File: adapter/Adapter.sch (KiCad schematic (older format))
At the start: 54 parts, among them J1 USB_B_Micro, J2 2040210-1, J3 USB_C_Receptacle, J4 Conn_01x05_Male, J5 Conn_01x03_Male, Q1 IRLML2244TRPBF, SW1 RESET, SW2 BOOT, U2 LD1117S33TR, U3 STM32F072C8Tx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

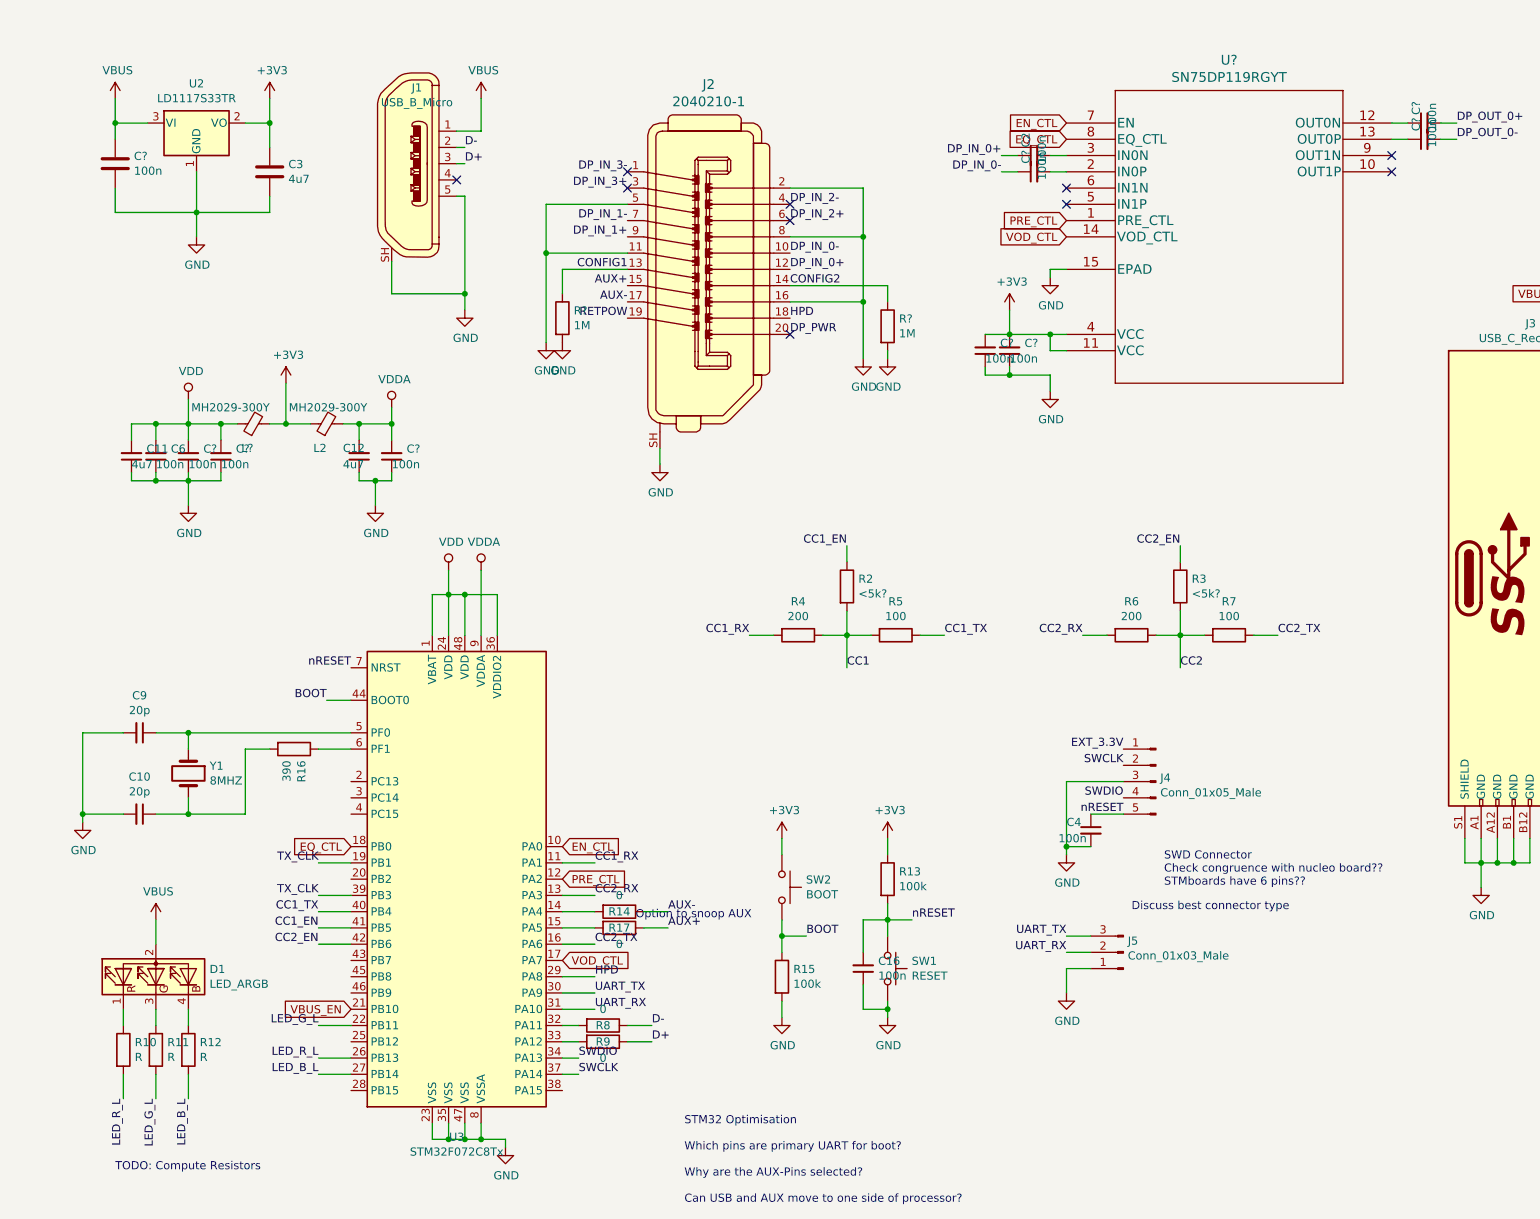
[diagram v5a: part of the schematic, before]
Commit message: cleared all order number for Arrow
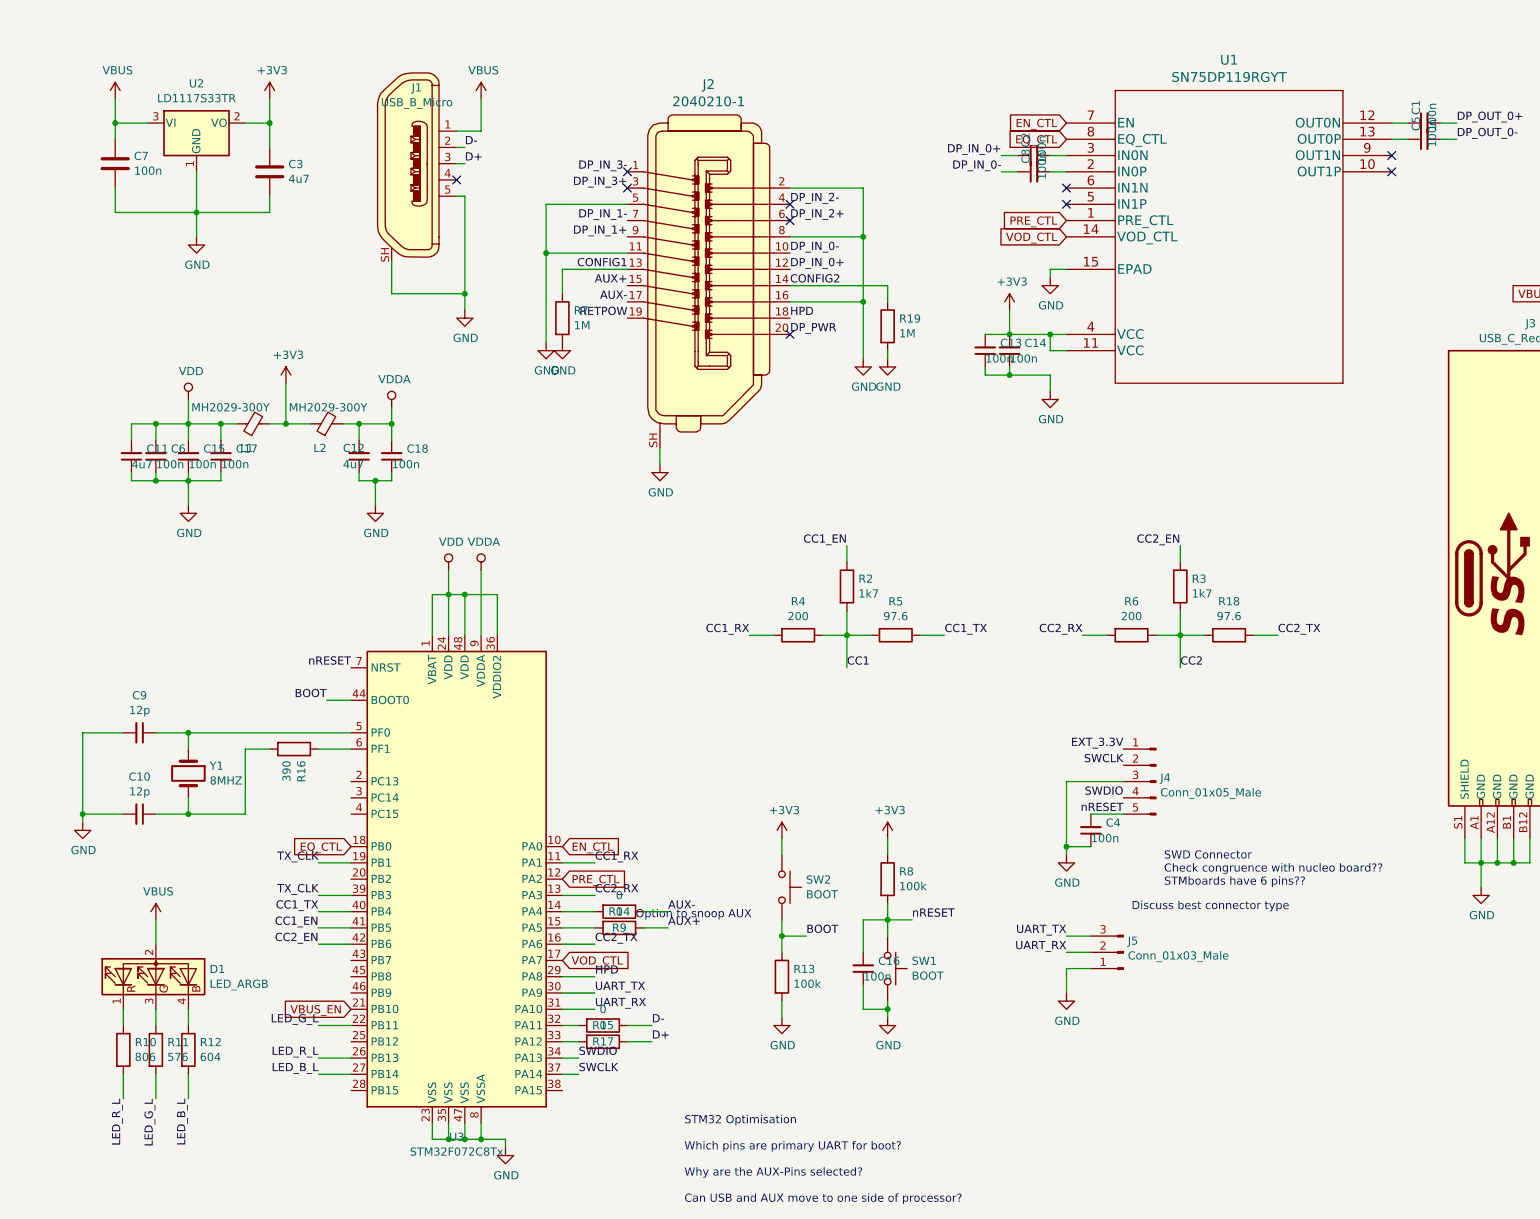
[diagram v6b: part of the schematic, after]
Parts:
- removed R?: 1M, symbol Device:R
- added R18: 97.6, Resistor_SMD:R_0603_1608Metric_Pad1.05x0.95mm_HandSolder, symbol Device:R
- C10, C9: value 20p -> 12p; MFP CC0603JRNPO9BN120 -> CL10C120JB8NNNC; S2PN (none) -> CL10C120JB8NNNC
- C16, C4: S2PN (none) -> CL10F104ZO8NNNC
- D1: S2PN (none) -> CLVBA-FKA-CAEDH8BBB7a363
- R1: S2PN (none) -> CRCW0603100KJNEAC
- R10: value R -> 806; MFP (none) -> RC0603FR-07806RL; S2PN (none) -> RC0603FR-07806RL
- R11: value R -> 576; MFP (none) -> RMCF0603FT576R; S2PN (none) -> RMCF0603FT576R
- R12: value R -> 604; MFP (none) -> RC0603FR-07604RL; S2PN (none) -> RC0603FR-07604RL
- R13: MFP RC0603FR-13100KL -> (none); S2PN (none) -> CRCW0603100KJNEAC
- R14, R17, R9: MFP (none) -> RC0603JR-070RL; S2PN (none) -> RC0603JR-070RL
- R15: value 100k -> 0; MFP RC0603FR-13100KL -> RC0603JR-070RL; S2PN (none) -> RC0603JR-070RL
- R16: MFP (none) -> RC0603JR-07390RL; S2PN (none) -> RC0603JR-07390RL
- R19: renamed from R?; footprint (none) -> Resistor_SMD:R_0603_1608Metric_Pad1.05x0.95mm_HandSolder; MFP (none) -> AC0603JR-071ML; S2PN RC0603FR-101ML -> AC0603JR-071ML
- R2, R3: value <5k? -> 1k7; MFP (none) -> RC0603FR-071K69L; S2PN (none) -> RC0603FR-071K69L
- R4, R6: MFP (none) -> RC0603FR-07200RL; S2PN (none) -> RC0603FR-07200RL
- R5: value 100 -> 97.6; MFP (none) -> RC0603FR-0797R6L; S2PN (none) -> RC0603FR-0797R6L
- R7: value 100 -> 1M; MFP (none) -> AC0603JR-071ML; S2PN (none) -> AC0603JR-071ML
- R8: value 0 -> 100k; S2PN (none) -> CRCW0603100KJNEAC
- SW1: value RESET -> BOOT; S2PN (none) -> EVQ-PLMA15
- SW2: S2PN (none) -> EVQ-PLMA15
- U2: MFP LD1117S33TR -> LD1117S33CTR; S2PN LD1117S33TR -> LD1117S33CTR
- U3: S2PN (none) -> STM32F072CBT6
- Y1: MFP 7A-8.000MAAE-T -> (none); S2PN (none) -> 7A-8.000MAAE-T
- gave numbers to parts that had none: 11
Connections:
- net +3V3: now also R8.1; no longer R13.1
- net AUX+: now also R9.1; no longer R17.1
- net BOOT: now also R13.1; no longer R15.1
- net CC2: now also R18.2; no longer R7.2
- net CC2_TX: now also R18.1; no longer R7.1
- net CONFIG1: now also R7.1
- net D+: now also R17.1; no longer R9.1
- net D-: now also R15.1; no longer R8.1
- net GND: now also C4.1, R13.2, R7.2; no longer C4.2, R15.2
- net nRESET: now also C4.2, R8.2; no longer C4.1, R13.2
- net at U3.15 (PA5): now also R9.2; no longer R17.2
- net at U3.32 (PA11): now also R15.2; no longer R8.2
- net at U3.33 (PA12): now also R17.2; no longer R9.2
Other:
- note removed: "TODO: Compute Resistors\n"

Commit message: placement mostly done
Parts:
- added MH1, MH2, MH3, MH4: MountingHole, MountingHole:MountingHole_2.5mm, symbol Mechanical:MountingHole
- J4: footprint Connector_Molex:Molex_PicoBlade_53047-0510_1x05_P1.25mm_Vertical -> Connector_PinHeader_2.54mm:PinHeader_1x05_P2.54mm_Horizontal
- J5: footprint Connector_Molex:Molex_PicoBlade_53047-0310_1x03_P1.25mm_Vertical -> Connector_PinHeader_2.54mm:PinHeader_1x03_P2.54mm_Horizontal
- SW1: value BOOT -> RESET
- U2: footprint Package_TO_SOT_SMD:SOT-223 -> Package_TO_SOT_SMD:SOT-223-3_TabPin2
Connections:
- wire segments 222 -> 225
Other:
- note added: "STM32 Optimisation\n\nWhich pins are primary UART for boot?\n\nWhy are the AUX-Pins selected?\n\nCan USB and AUX move to one side of processor? -> No, USB is fixed and not near the analog pins\n\nWhere can TX_CLK move?\nTX_CLKIN: SPI1_SCK"
- note removed: "STM32 Optimisation\n\nWhich pins are primary UART for boot?\n\nWhy are the AUX-Pins selected?\n\nCan USB and AUX move to one side of processor?"
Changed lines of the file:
@@
 Text GLabel 6700 1100 0    50   Input ~ 0
 EN_CTL
+Text Label 6300 1300 2    50   ~ 0
+DP_IN_0-
 Text Label 6300 1400 2    50   ~ 0
-DP_IN_0-
-Text Label 6300 1300 2    50   ~ 0
 DP_IN_0+
 $Comp
@@
 	1    0    0    -1
 $EndComp
+Text Label 9100 1200 0    50   ~ 0
+DP_OUT_0+
 Text Label 9100 1100 0    50   ~ 0
-DP_OUT_0+
-Text Label 9100 1200 0    50   ~ 0
 DP_OUT_0-
 NoConn ~ 10050 3900
@@
 F 0 "U2" H 1350 1342 50  0000 C CNN
 F 1 "LD1117S33TR" H 1350 1251 50  0000 C CNN
-F 2 "Package_TO_SOT_SMD:SOT-223" H 1350 1350 50  0001 C CIN
+F 2 "Package_TO_SOT_SMD:SOT-223-3_TabPin2" H 1350 1350 50  0001 C CIN
 F 3 "https://www.diodes.com/assets/Datasheets/AZ1117.pdf" H 1350 1100 50  0001 C CNN
 F 4 "LD1117S33CTR" H 1350 1100 50  0001 C CNN "MFP"
@@
 F 0 "J4" H 7223 5173 50  0000 R CNN
 F 1 "Conn_01x05_Male" H 7223 5082 50  0000 R CNN
-F 2 "Connector_Molex:Molex_PicoBlade_53047-0510_1x05_P1.25mm_Vertical" H 7250 5150 50  0001 C CNN
+F 2 "Connector_PinHeader_2.54mm:PinHeader_1x05_P2.54mm_Horizontal" H 7250 5150 50  0001 C CNN
 F 3 "~" H 7250 5150 50  0001 C CNN
 	1    7250 5150
@@
 Text Label 2100 6050 2    50   ~ 0
 CC1_EN
-Text Label 3800 5650 0    50   ~ 0
+Text Label 2100 5550 2    50   ~ 0
 CC1_RX
 Wire Wire Line
 	3800 5650 3600 5650
-Text Label 2100 6150 2    50   ~ 0
+Text Label 2100 5750 2    50   ~ 0
 CC2_EN
-Text Label 3800 5850 0    50   ~ 0
+Text Label 2100 5650 2    50   ~ 0
 CC2_RX
 Wire Wire Line
@@
 Wire Wire Line
 	3800 6050 3600 6050
-Text Label 2100 5650 2    50   ~ 0
+Text Label 2100 6350 2    50   ~ 0
 TX_CLK
 Text Label 2100 5850 2    50   ~ 0
 TX_CLK
-Text GLabel 3600 6250 2    50   Input ~ 0
+Text GLabel 3800 5850 2    50   Input ~ 0
 VOD_CTL
 Text Label 2100 6650 2    50   ~ 0
@@
 Wire Wire Line
 	1100 6000 1100 6150
-Text GLabel 2300 5550 0    50   Input ~ 0
+Text GLabel 3800 5650 2    50   Input ~ 0
 EQ_CTL
 Text GLabel 3600 5550 2    50   Input ~ 0
@@
 	3600 6850 3700 6850
 Wire Wire Line
-	2100 5650 2300 5650
-Wire Wire Line
 	2100 5850 2300 5850
 $Comp
@@
 	4100 5950 4250 5950
 Wire Wire Line
-	2100 6150 2300 6150
+	2100 5750 2300 5750
 Wire Wire Line
 	2100 6050 2300 6050
@@
 F 0 "J5" H 7023 6130 50  0000 R CNN
 F 1 "Conn_01x03_Male" H 7023 6221 50  0000 R CNN
-F 2 "Connector_Molex:Molex_PicoBlade_53047-0310_1x03_P1.25mm_Vertical" H 7050 6200 50  0001 C CNN
+F 2 "Connector_PinHeader_2.54mm:PinHeader_1x03_P2.54mm_Horizontal" H 7050 6200 50  0001 C CNN
 F 3 "~" H 7050 6200 50  0001 C CNN
 	1    7050 6200
@@
 Text Notes 4050 6000 0    50   ~ 0
 Option to snoop AUX
-Text Notes 4350 7750 0    50   ~ 0
-STM32 Optimisation\n\nWhich pins are primary UART for boot?\n\nWhy are the AUX-Pins selected?\n\nCan USB and AUX move to one side of processor?
+Text Notes 3750 8700 0    50   ~ 0
+STM32 Optimisation\n\nWhich pins are primary UART for boot?\n\nWhy are the AUX-Pins selected?\n\nCan USB and AUX move to one side of processor? -> No, USB is fixed and not near the analog pins\n\nWhere can TX_CLK move?\nTX_CLKIN: SPI1_SCK
 $Comp
 L Device:R R19
@@
 P 5600 6300
 F 0 "SW1" V 5554 6448 50  0000 L CNN
-F 1 "BOOT" V 5645 6448 50  0000 L CNN
+F 1 "RESET" V 5645 6448 50  0000 L CNN
 F 2 "EVQPLMA15:EVQPLMA15" H 5600 6500 50  0001 C CNN
 F 3 "" H 5600 6500 50  0001 C CNN
@@
 	0    1    1    0
 $EndComp
+$Comp
+L Mechanical:MountingHole MH1
+U 1 1 5C603BB2
+P 10300 5850
+F 0 "MH1" H 10400 5896 50  0000 L CNN
+F 1 "MountingHole" H 10400 5805 50  0000 L CNN
+F 2 "MountingHole:MountingHole_2.5mm" H 10300 5850 50  0001 C CNN
+F 3 "~" H 10300 5850 50  0001 C CNN
+	1    10300 5850
+	1    0    0    -1
+$EndComp
+$Comp
+L Mechanical:MountingHole MH2
+U 1 1 5C603DAD
+P 10300 6050
+F 0 "MH2" H 10400 6096 50  0000 L CNN
+F 1 "MountingHole" H 10400 6005 50  0000 L CNN
+F 2 "MountingHole:MountingHole_2.5mm" H 10300 6050 50  0001 C CNN
+F 3 "~" H 10300 6050 50  0001 C CNN
+	1    10300 6050
+	1    0    0    -1
+$EndComp
+$Comp
+L Mechanical:MountingHole MH3
+U 1 1 5C612305
+P 10300 6250
+F 0 "MH3" H 10400 6296 50  0000 L CNN
+F 1 "MountingHole" H 10400 6205 50  0000 L CNN
+F 2 "MountingHole:MountingHole_2.5mm" H 10300 6250 50  0001 C CNN
+F 3 "~" H 10300 6250 50  0001 C CNN
+	1    10300 6250
+	1    0    0    -1
+$EndComp
+$Comp
+L Mechanical:MountingHole MH4
+U 1 1 5C6337DC
+P 10300 6450
+F 0 "MH4" H 10400 6496 50  0000 L CNN
+F 1 "MountingHole" H 10400 6405 50  0000 L CNN
+F 2 "MountingHole:MountingHole_2.5mm" H 10300 6450 50  0001 C CNN
+F 3 "~" H 10300 6450 50  0001 C CNN
+	1    10300 6450
+	1    0    0    -1
+$EndComp
+Wire Wire Line
+	3800 6250 3600 6250
+Wire Wire Line
+	2100 5650 2300 5650
+Wire Wire Line
+	2100 5550 2300 5550
+Wire Wire Line
+	2100 6350 2300 6350
 $EndSCHEMATC

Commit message: first fully routed
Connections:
- no-connect marks 16 -> 17
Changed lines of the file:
@@
 Text GLabel 9850 2150 0    50   Input ~ 0
 VBUS_EN
-Text GLabel 2300 6550 0    50   Input ~ 0
+Text GLabel 2300 6450 0    50   Input ~ 0
 VBUS_EN
 $Comp
@@
 Wire Wire Line
 	2100 6350 2300 6350
+NoConn ~ 3350 3250
 $EndSCHEMATC
